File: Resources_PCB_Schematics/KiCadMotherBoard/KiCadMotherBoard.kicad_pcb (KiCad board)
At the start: 2 copper layers, 97 x 69 mm, 25 parts, among them J1 Conn_01x02_Male, J10 Conn_01x02_Male_DATA, J11 Conn_01x02_Male_DATA, J12 Conn_01x02_Male_DATA, J13 Conn_01x02_Male_DATA, J14 Conn_01x02_Male_DATA, J15 Conn_01x02_Male_DATA, J16 Conn_01x02_Male_DATA, J2 Conn_01x02_Male, J3 Conn_01x02_Male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

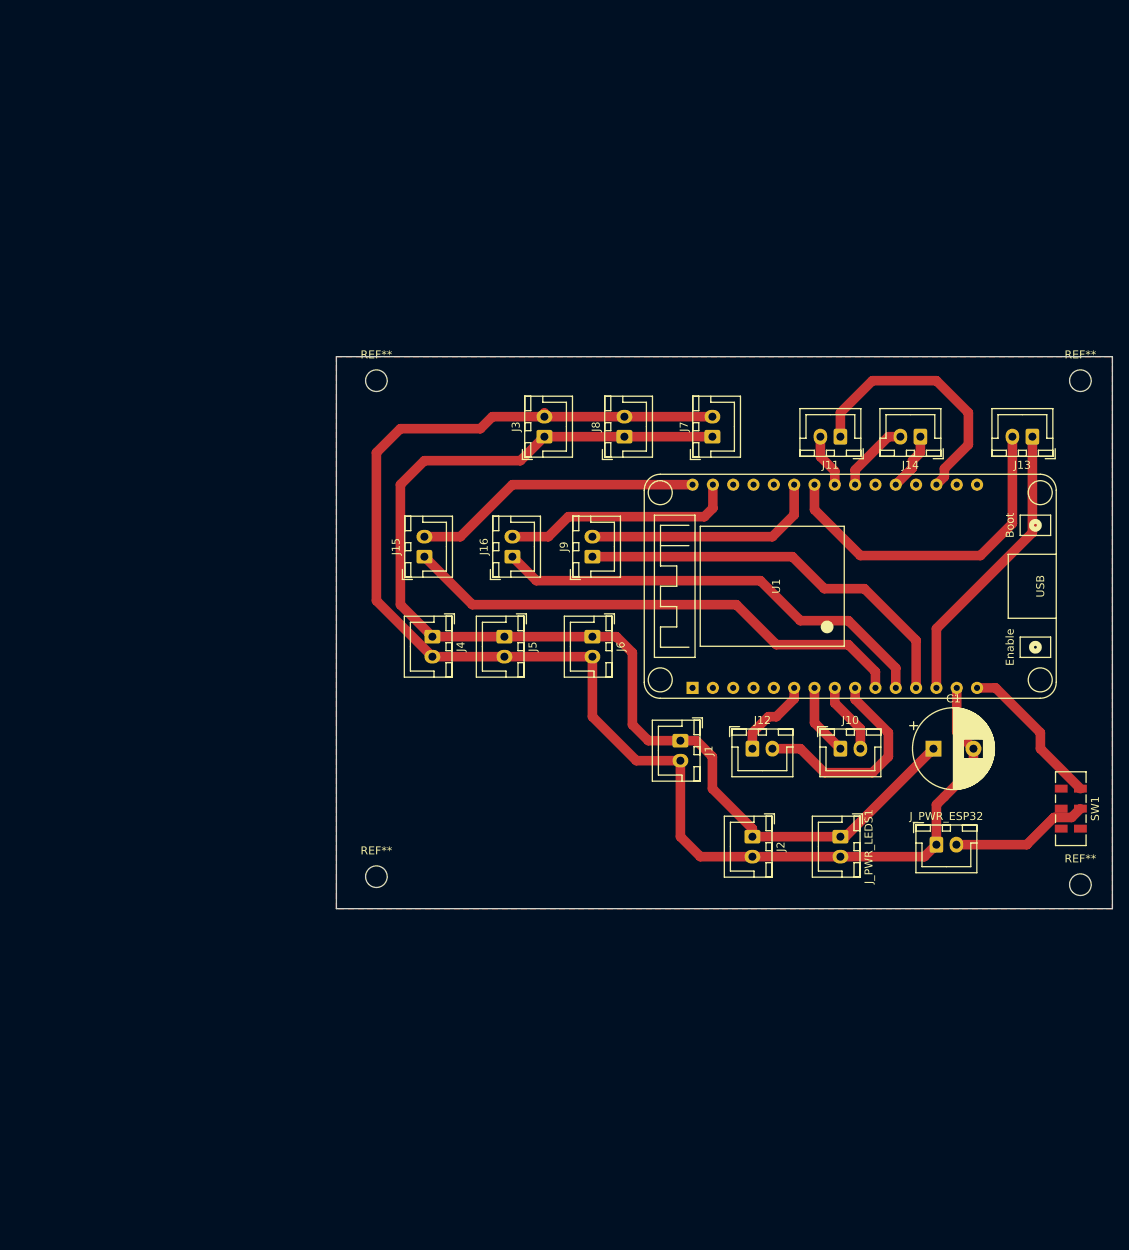
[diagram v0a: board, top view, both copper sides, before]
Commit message: Moved to adafruit Neopixel Library, more tests to do. Fast led don't work
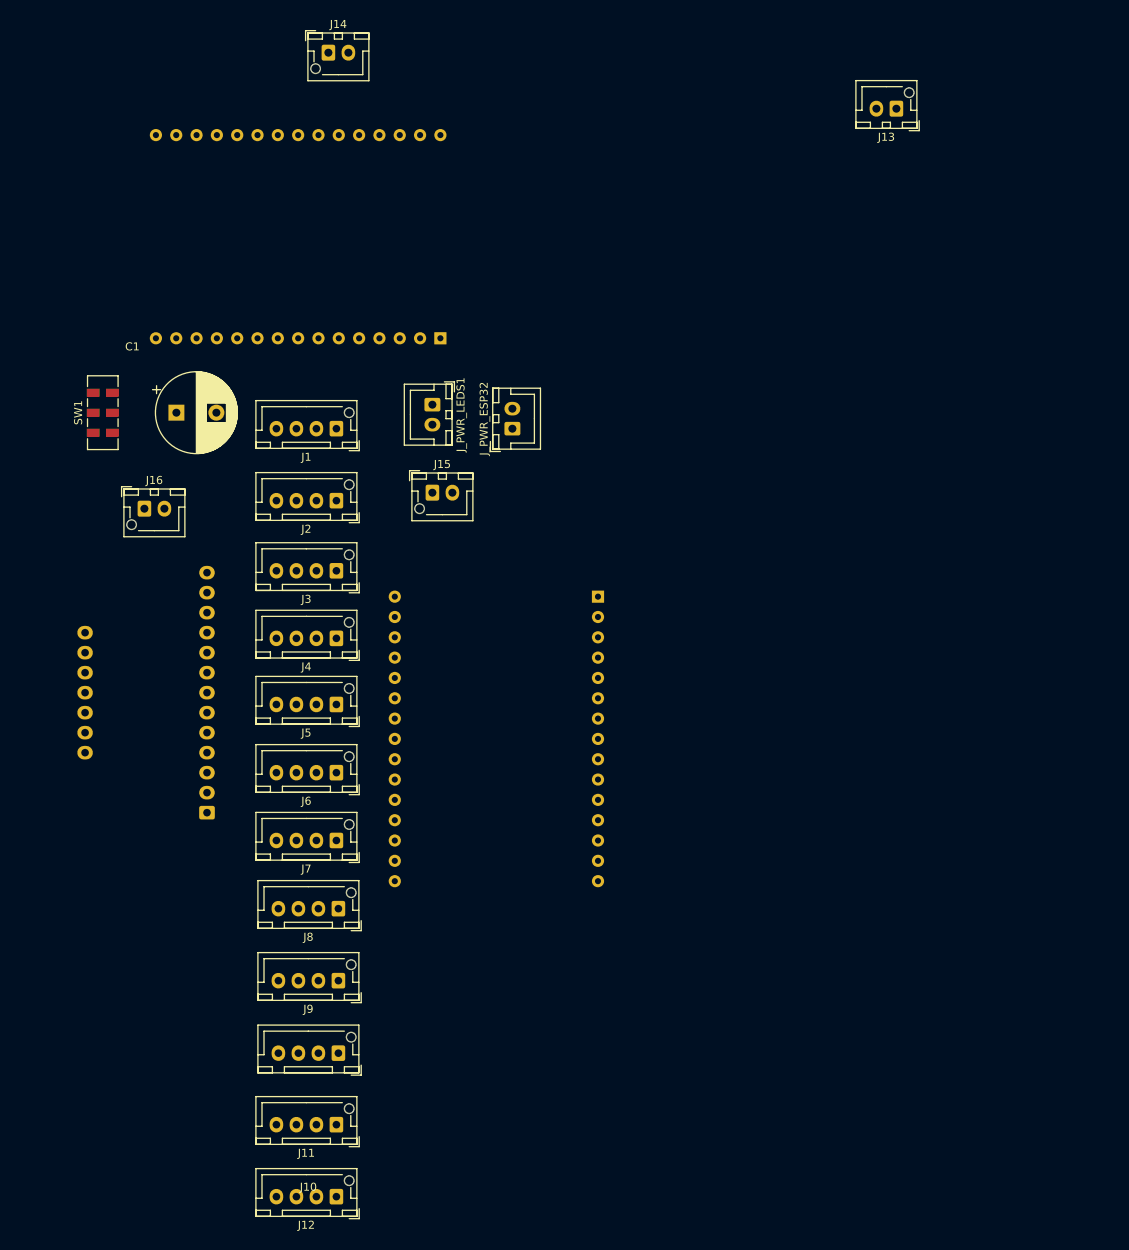
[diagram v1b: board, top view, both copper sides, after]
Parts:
- removed REF** (x4): MountingHole_2.7mm_M2.5_ISO7380, MountingHole:MountingHole_2.7mm_M2.5_ISO7380
- added U2: LED_CONTROLLER, ESP32_devkit_v1:esp32_devkit_v1_doit, B.Cu at (122.5, 98.1)
- added U3: MPR121QR2, mpr121_test-3:custom-mpr121, B.Cu at (86.3, 125.1)
- J1, J2, J3, J4, J5, J6, J7, J8: value Conn_01x02_Male -> Conn_01x04_Male; footprint Connector_JST:JST_XH_B2B-XH-A_1x02_P2.50mm_Vertical -> Connector_JST:JST_XH_B4B-XH-AM_1x04_P2.50mm_Vertical
- J10, J11, J12, J9: value Conn_01x02_Male_DATA -> Conn_01x04_Male; footprint Connector_JST:JST_XH_B2B-XH-A_1x02_P2.50mm_Vertical -> Connector_JST:JST_XH_B4B-XH-AM_1x04_P2.50mm_Vertical
- J13, J14, J15, J16: value Conn_01x02_Male_DATA -> SDA_SCL_BRIDGE; footprint Connector_JST:JST_XH_B2B-XH-A_1x02_P2.50mm_Vertical -> Connector_JST:JST_XH_B2B-XH-AM_1x02_P2.50mm_Vertical
- U1: value ESP32_DevKit_V1_DOIT -> ESP32_DevKit_V1_DOIT_MAIN_CONTROLLER; moved to B.Cu
- moved SW1 130.7 mm to (73.3, 75.1), turned to 90 degrees
- moved J11 106.6 mm to (102.5, 164.1)
- moved C1 103.5 mm to (82.5, 75.1)
- moved J14 88.2 mm to (101.5, 30.1), turned to 0 degrees
- moved J12 76.4 mm to (102.5, 173.1), turned to 180 degrees
- moved J_PWR_LEDS1 74.3 mm to (114.5, 74.1)
- moved J_PWR_ESP32 74.2 mm to (124.5, 77.1), turned to 90 degrees
- moved J10 73.4 mm to (102.8, 155.2), turned to 180 degrees
- moved J8 69.0 mm to (102.8, 137.1), turned to 180 degrees
- moved J7 69.0 mm to (102.5, 128.6), turned to 180 degrees
- moved J2 66.8 mm to (102.5, 86.1), turned to 180 degrees
- moved J9 61.8 mm to (102.8, 146.1), turned to 180 degrees
- moved J1 58.1 mm to (102.5, 77.1), turned to 180 degrees
- moved U1 53.9 mm to (115.5, 53.1)
- moved J16 46.4 mm to (78.5, 87.1), turned to 0 degrees
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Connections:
- J1 pad 1: +5V -> /LED_P32
- J10 pad 1: /T8 -> /LED_P5
- J10 pad 2: /LED1 -> GND
- J11 pad 1: /T3 -> /LED_P12
- J11 pad 2: /LED7 -> GND
- J12 pad 1: /T9 -> /LED_P13
- J12 pad 2: /LED2 -> GND
- J13 pad 1: /T4 -> /SDA
- J13 pad 2: /LED6 -> /SCL
- J14 pad 1: /T0 -> /SDA
- J14 pad 2: /LED8 -> /SCL
- J15 pad 1: /T7 -> /SDA
- J15 pad 2: /LED3 -> /SCL
- J16 pad 1: /T6 -> /SDA
- J16 pad 2: /LED4 -> /SCL
- J2 pad 1: +5V -> /LED_P33
- J3 pad 1: +5V -> /LED_P25
- J4 pad 1: +5V -> /LED_P26
- J5 pad 1: +5V -> /LED_P27
- J6 pad 1: +5V -> /LED_P14
- J7 pad 1: +5V -> /LED_P23
- J8 pad 1: +5V -> /LED_P19
- J9 pad 1: /T5 -> /LED_P18
- J9 pad 2: /LED5 -> GND
- U1 pad 10: /T7 -> unconnected-(U1-Pad10)
- U1 pad 11: /T6 -> unconnected-(U1-Pad11)
- U1 pad 12: /T5 -> unconnected-(U1-Pad12)
- U1 pad 13: /T4 -> unconnected-(U1-Pad13)
- U1 pad 16: unconnected-(U1-Pad16) -> /MAIN_CONTROLLER_3V3
- U1 pad 18: /T3 -> unconnected-(U1-Pad18)
- U1 pad 19: /(T2) -> unconnected-(U1-Pad19)
- U1 pad 20: /T0 -> unconnected-(U1-Pad20)
- U1 pad 22: /LED8 -> unconnected-(U1-Pad22)
- U1 pad 23: /LED7 -> unconnected-(U1-Pad23)
- U1 pad 24: /LED6 -> unconnected-(U1-Pad24)
- U1 pad 25: /LED5 -> unconnected-(U1-Pad25)
- U1 pad 26: unconnected-(U1-Pad26) -> /SDA
- U1 pad 29: /LED4 -> /SCL
- U1 pad 30: /LED3 -> unconnected-(U1-Pad30)
- U1 pad 6: /T9 -> unconnected-(U1-Pad6)
- U1 pad 7: /T8 -> unconnected-(U1-Pad7)
- U1 pad 8: /LED1 -> unconnected-(U1-Pad8)
- U1 pad 9: /LED2 -> unconnected-(U1-Pad9)
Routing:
- net GND: track 179.1 -> 0.00 mm
- net +5V: track 147.9 -> 0.00 mm
- net /T7: track 64.4 -> 0.00 mm
- net /T6: track 56.2 -> 0.00 mm
- net /T5: track 50.7 -> 0.00 mm
- net /LED6: track 42.8 -> 0.00 mm
- net /T4: track 38.0 -> 0.00 mm
- net /LED3: track 36.2 -> 0.00 mm
- net /T3: track 33.0 -> 0.00 mm
- net /LED5: track 30.1 -> 0.00 mm
- net /LED4: track 29.5 -> 0.00 mm
- net /LED2: track 26.9 -> 0.00 mm
- net VCC: track 19.3 -> 0.00 mm
- net Net-(J_PWR_ESP32-Pad2): track 17.4 -> 0.00 mm
- net /T9: track 10.3 -> 0.00 mm
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- removed copper zone on F.Cu, net GND
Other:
- board outline removed
- board text added: "TESTER SDA/SCL sur 22/1"
- board text removed: "ETERN=LED-POWER"
- board text removed: "INTERN=LED_DATA"

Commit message: implementing
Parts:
- removed J15, J16: SDA_SCL_BRIDGE, Connector_JST:JST_XH_B2B-XH-AM_1x02_P2.50mm_Vertical
- removed U2: LED_CONTROLLER, ESP32_devkit_v1:esp32_devkit_v1_doit
- added ?: , , F.Cu at (86.5, 111.1)
- added ?: , , F.Cu at (118.5, 111.1)
- added ?: , , F.Cu at (67.5, 61.1)
- added ?: , , F.Cu at (129.5, 61.1)
- added REF**: Pin_D1.0mm_L10.0mm, Connector_Pin:Pin_D1.0mm_L10.0mm, F.Cu at (67.5, 165.1)
- added REF**: Pin_D1.0mm_L10.0mm, Connector_Pin:Pin_D1.0mm_L10.0mm, F.Cu at (129.5, 165.1)
- moved J14 114.0 mm to (86.5, 143.1)
- moved J13 110.1 mm to (120.5, 134.1), turned to 0 degrees
- moved J_PWR_LEDS1 92.3 mm to (86.5, 162.1), turned to 0 degrees
- moved U1 87.9 mm to (78.5, 132.8), turned to 0 degrees
- moved C1 84.5 mm to (77.5, 159.5), turned to 90 degrees
- moved J_PWR_ESP32 39.3 mm to (86.5, 67.1), turned to 180 degrees
- moved U3 36.9 mm to (112.5, 99.1), turned to -90 degrees
- moved J9 13.9 mm to (98.0, 133.1), turned to 0 degrees
- moved J3 13.4 mm to (98.0, 82.2), turned to 0 degrees
- moved J8 13.4 mm to (98.0, 124.6), turned to 0 degrees
- moved J4 13.3 mm to (98.0, 90.8), turned to 0 degrees
- moved J7 13.3 mm to (98.0, 116.1), turned to 0 degrees
- moved J2 13.2 mm to (98.0, 73.7), turned to 0 degrees
- moved J5 13.1 mm to (98.0, 99.3), turned to 0 degrees
- moved J6 13.1 mm to (98.0, 107.9), turned to 0 degrees
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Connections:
- J1 pad 1: /LED_P32 -> /LED_P13
- J1 pad 4: /TOUCH12 -> /TOUCH3
- J10 pad 1: /LED_P5 -> /LED_P25
- J10 pad 4: /TOUCH2 -> /TOUCH12
- J11 pad 1: /LED_P12 -> /LED_P33
- J11 pad 4: /TOUCH3 -> /TOUCH11
- J12 pad 1: /LED_P13 -> /LED_P32
- J12 pad 4: /TOUCH4 -> /TOUCH10
- J2 pad 1: /LED_P33 -> /LED_P12
- J2 pad 4: /TOUCH11 -> /TOUCH2
- J3 pad 1: /LED_P25 -> /LED_P14
- J3 pad 4: /TOUCH10 -> /TOUCH1
- J4 pad 1: /LED_P26 -> /LED_P27
- J4 pad 4: /TOUCH9 -> /TOUCH4
- J5 pad 1: /LED_P27 -> /LED_P26
- J5 pad 4: /TOUCH8 -> /TOUCH5
- J6 pad 1: /LED_P14 -> /LED_P4
- J6 pad 4: /TOUCH7 -> /TOUCH6
- J7 pad 1: /LED_P23 -> /LED_P19
- J7 pad 4: /TOUCH6 -> /TOUCH7
- J8 pad 1: /LED_P19 -> /LED_P3
- J8 pad 4: /TOUCH5 -> /TOUCH8
- J9 pad 1: /LED_P18 -> /LED_P23
- J9 pad 4: /TOUCH1 -> /TOUCH9
- U1 pad 10: unconnected-(U1-Pad10) -> /LED_P27
- U1 pad 11: unconnected-(U1-Pad11) -> /LED_P14
- U1 pad 12: unconnected-(U1-Pad12) -> /LED_P12
- U1 pad 13: unconnected-(U1-Pad13) -> /LED_P13
- U1 pad 16: /MAIN_CONTROLLER_3V3 -> unconnected-(U1-Pad16)
- U1 pad 20: unconnected-(U1-Pad20) -> /LED_P4
- U1 pad 25: unconnected-(U1-Pad25) -> /LED_P19
- U1 pad 27: unconnected-(U1-Pad27) -> /LED_P3
- U1 pad 30: unconnected-(U1-Pad30) -> /LED_P23
- U1 pad 6: unconnected-(U1-Pad6) -> /LED_P32
- U1 pad 7: unconnected-(U1-Pad7) -> /LED_P33
- U1 pad 8: unconnected-(U1-Pad8) -> /LED_P25
- U1 pad 9: unconnected-(U1-Pad9) -> /LED_P26
- U3 pad 6: unconnected-(U3-Pad6) -> GND
- U3 pad 7: GND -> unconnected-(U3-Pad7)
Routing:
- net GND: track 0.00 -> 301.7 mm
- net VCC: track 0.00 -> 133.2 mm
- net +5V: track 0.00 -> 133.0 mm
- net /LED_P32: track 0.00 -> 60.0 mm
- net /LED_P33: track 0.00 -> 58.6 mm
- net /LED_P25: track 0.00 -> 58.4 mm
- net /LED_P13: track 0.00 -> 52.6 mm
- net /TOUCH10: track 0.00 -> 50.0 mm
- net /TOUCH3: track 0.00 -> 49.8 mm
- net /SDA: track 0.00 -> 48.6 mm
- net /LED_P12: track 0.00 -> 46.3 mm
- net /LED_P26: track 0.00 -> 44.7 mm
- net /LED_P14: track 0.00 -> 42.6 mm
- net /LED_P27: track 0.00 -> 40.2 mm
- net /TOUCH11: track 0.00 -> 37.9 mm
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- added copper zone on F.Cu, net GND
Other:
- board outline added: 72 x 113 mm
- board text added: "I2C"
- board text removed: "TESTER SDA/SCL sur 22/1"
